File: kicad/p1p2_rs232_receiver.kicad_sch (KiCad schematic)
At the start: 51 parts, among them J1 Raspberry_Pi_2_3, J2 PC MC_1,5_2-G-3.81, U1 LTV-817S, U2 LM317L_TO92, U3 Pico

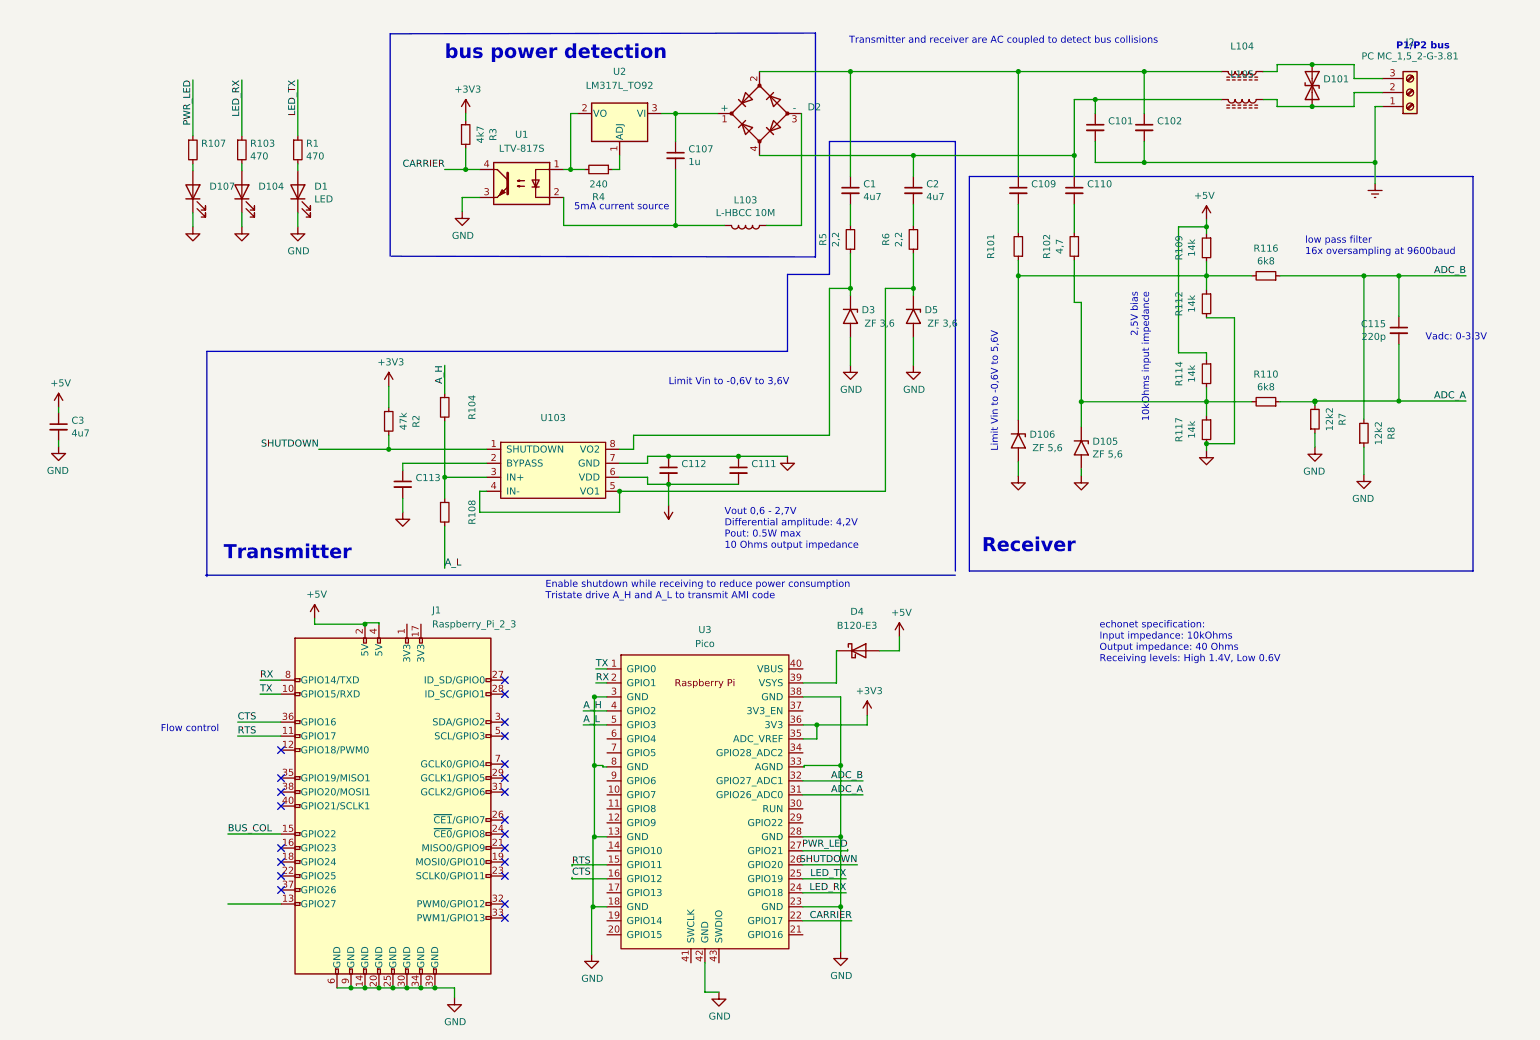
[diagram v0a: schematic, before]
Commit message: kicad: Minor fixes
Signed-off-by: Patrick Rudolph <rudolphpatrick05@gmail.com>
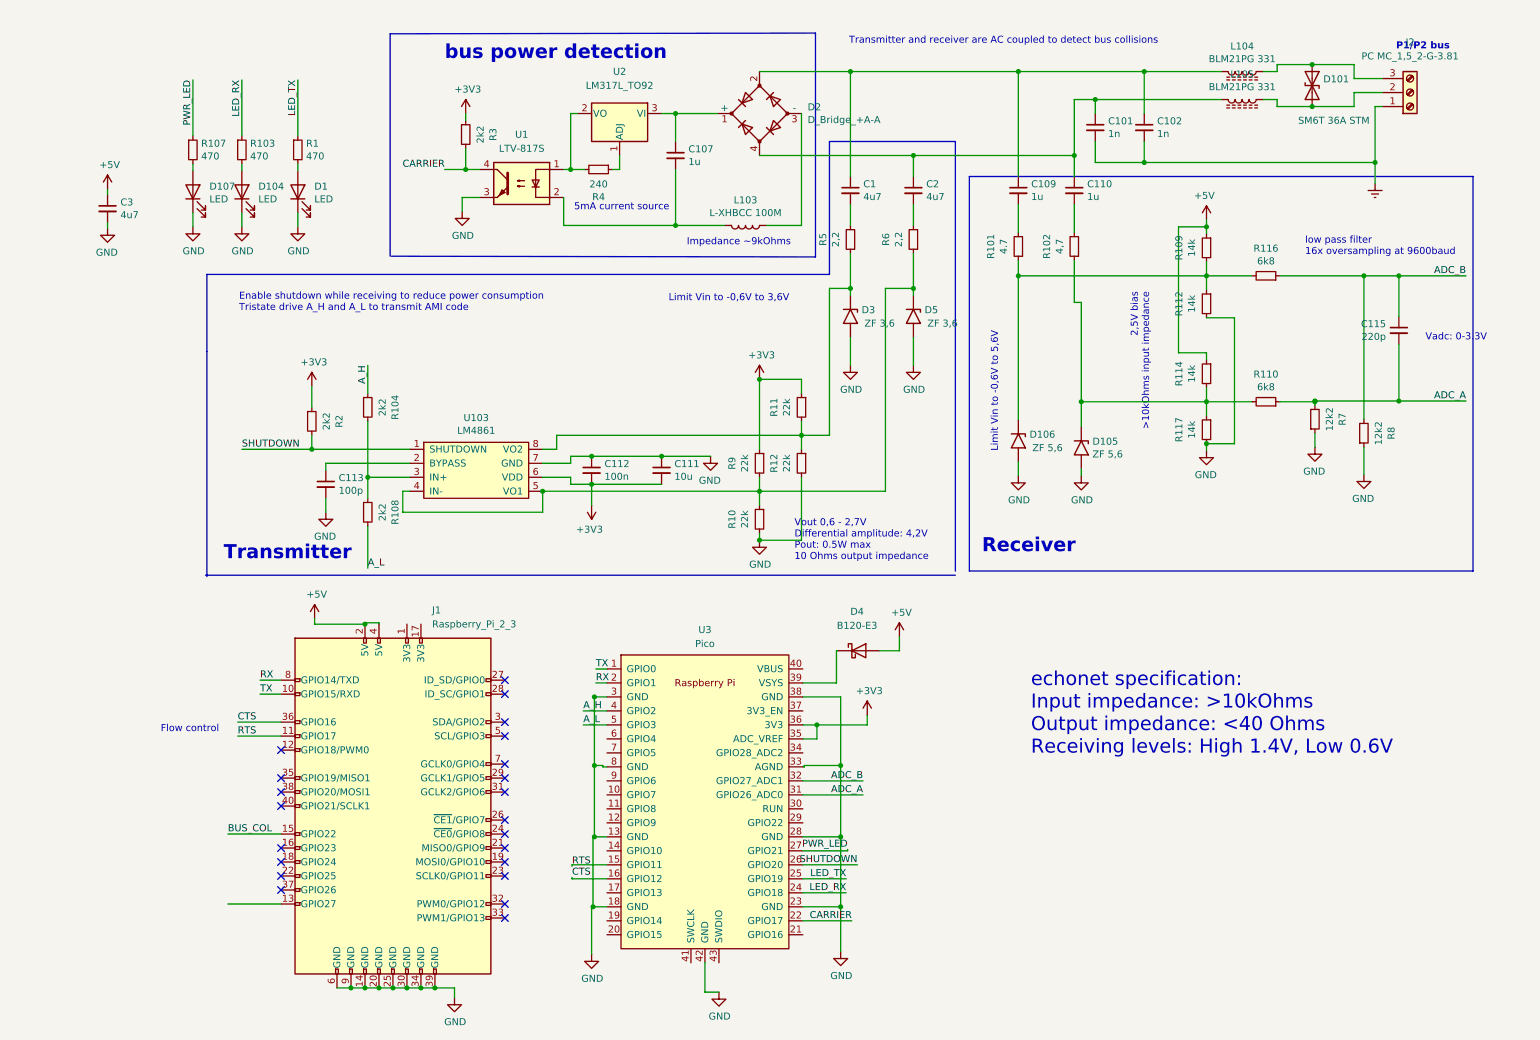
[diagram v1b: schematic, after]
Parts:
- added R10, R11, R12, R9: 22k, Resistor_SMD:R_0805_2012Metric_Pad1.20x1.40mm_HandSolder, symbol Device:R_Small
- C101, C102: value (none) -> 1n; footprint (none) -> Capacitor_SMD:C_0603_1608Metric_Pad1.08x0.95mm_HandSolder
- C109, C110: value (none) -> 1u; footprint (none) -> Capacitor_SMD:C_1210_3225Metric_Pad1.33x2.70mm_HandSolder
- C111: value (none) -> 10u; footprint (none) -> Capacitor_SMD:C_1210_3225Metric_Pad1.33x2.70mm_HandSolder
- C112: value (none) -> 100n; footprint (none) -> Capacitor_SMD:C_0805_2012Metric_Pad1.18x1.45mm_HandSolder
- C113: value (none) -> 100p; footprint (none) -> Capacitor_SMD:C_0603_1608Metric_Pad1.08x0.95mm_HandSolder
- D101: value (none) -> SM6T 36A STM; footprint (none) -> Diode_SMD:D_SMB
- D104, D107: value (none) -> LED; footprint (none) -> LED_SMD:LED_0805_2012Metric_Pad1.15x1.40mm_HandSolder
- D2: value (none) -> D_Bridge_+A-A; footprint (none) -> Diode_THT:Diode_Bridge_Round_D9.0mm
- L103: value L-HBCC 10M -> L-XHBCC 100M
- L104, L105: value (none) -> BLM21PG 331; footprint (none) -> Inductor_SMD:L_0805_2012Metric_Pad1.15x1.40mm_HandSolder
- R101: value (none) -> 4.7; footprint (none) -> Resistor_SMD:R_1206_3216Metric_Pad1.30x1.75mm_HandSolder
- R104, R108: value (none) -> 2k2; footprint (none) -> Resistor_SMD:R_0805_2012Metric_Pad1.20x1.40mm_HandSolder
- R107: value (none) -> 470; footprint (none) -> Resistor_SMD:R_0805_2012Metric_Pad1.20x1.40mm_HandSolder
- R2: value 47k -> 2k2
- R3: value 4k7 -> 2k2
- U103: value (none) -> LM4861
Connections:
- net +3V3: now also R11.1, R9.1
- net GND: now also R10.2, R12.2
- net at D5.1 (A1), R6.1, U103.4 (IN-)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: now also R10.1, R9.2
- net at D3.1 (A1), R5.1, U103.8 (VO2): now also R11.2, R12.1
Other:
- note added: "2,5V bias >10kOhms input impedance"
- note added: "Impedance ~9kOhms"
- note added: "echonet specification: Input impedance: >10kOhms Output impedance: <40 Ohms Receiving levels: High 1.4V, Low 0.6V"
- note removed: "2,5V bias 10kOhms input impedance"
- note removed: "echonet specification: Input impedance: 10kOhms Output impedance: 40 Ohms Receiving levels: High 1.4V, Low 0.6V"
- moved on the sheet: C111, C112, C113, C3, R104, R108, R2, U103

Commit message: kicad: Update schematics
- Add common mode choke
- Use gain 5 for OpAmp
  The OpAmp is not stable at unity gain.
  The OpAmp is not stable with high impedance load (unconnected P1/P2 bus).
- Use OpAmp in inverting operation mode instead voltage follower mode
- Add 'DNP' pull down and capacitor on OpAmp feedback
  TODO: Figure out if required for stability.
- Replace DC bus level detection
- Use external precision 3.0V voltage shunt as ADC voltage
- Use 3.0V as bias voltage to reduce noise
- Add Pico reset button

Signed-off-by: Patrick Rudolph <rudolphpatrick05@gmail.com>
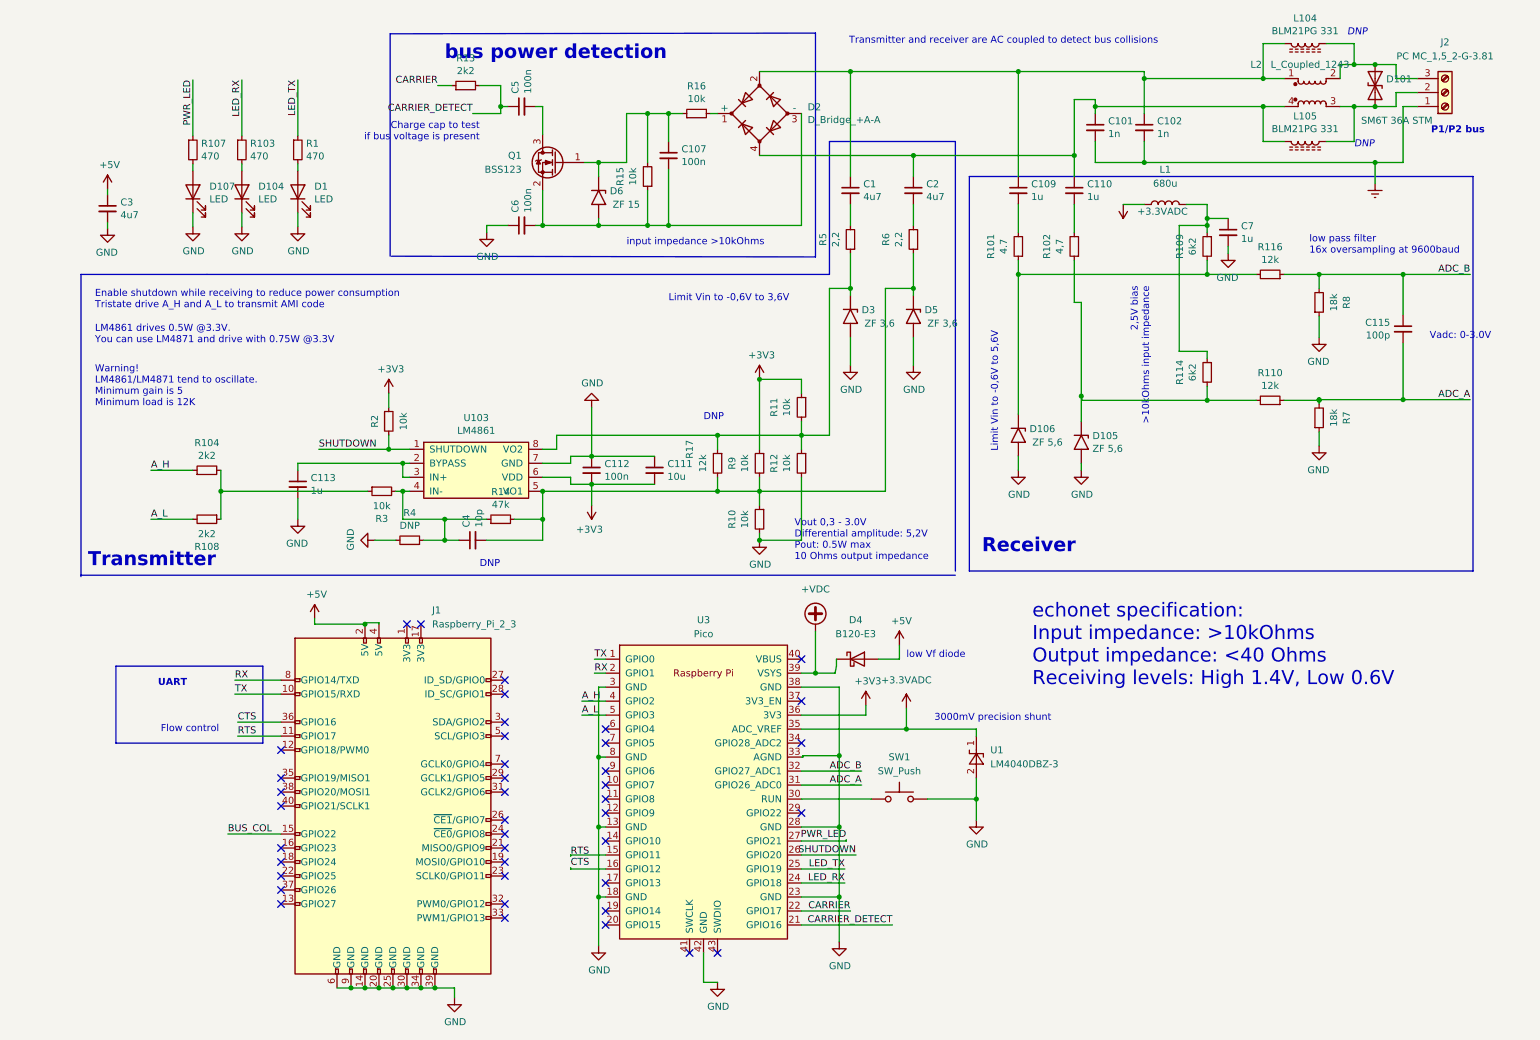
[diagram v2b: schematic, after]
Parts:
- removed L103: L-XHBCC 100M, Inductor_THT:L_Axial_L14.0mm_D4.5mm_P5.08mm_Vertical_Fastron_LACC, symbol Device:L
- removed R112, R117: 14k, Resistor_SMD:R_0805_2012Metric_Pad1.20x1.40mm_HandSolder, symbol Device:R_Small
- removed U1: LTV-817S, Package_DIP:SMDIP-4_W9.53mm, symbol Isolator:LTV-817S
- removed U2: LM317L_TO92, Package_TO_SOT_THT:TO-92_Inline, symbol Regulator_Linear:LM317L_TO92
- added C4: 10p, Capacitor_SMD:C_0805_2012Metric_Pad1.18x1.45mm_HandSolder, symbol Device:C_Small
- added C5, C6: 100n, Capacitor_SMD:C_0805_2012Metric_Pad1.18x1.45mm_HandSolder, symbol Device:C_Small
- added C7: 1u, Capacitor_SMD:C_1210_3225Metric_Pad1.33x2.70mm_HandSolder, symbol Device:C_Small
- added D6: ZF 15, Diode_THT:D_5W_P5.08mm_Vertical_AnodeUp, symbol Diode:SM6T24A
- added L1: 680u, Inductor_SMD:L_1210_3225Metric_Pad1.42x2.65mm_HandSolder, symbol Device:L
- added L2: L_Coupled_1243, B82790C0:L_CommonMode_TDK_B82790C0, symbol Device:L_Coupled_1243
- added Q1: BSS123, Package_TO_SOT_SMD:SOT-23, symbol Transistor_FET:BSS123
- added R13: 2k2, Resistor_SMD:R_0805_2012Metric_Pad1.20x1.40mm_HandSolder, symbol Device:R_Small
- added R14: 47k, Resistor_SMD:R_0805_2012Metric_Pad1.20x1.40mm_HandSolder, symbol Device:R_Small
- added R15, R16: 10k, Resistor_SMD:R_0805_2012Metric_Pad1.20x1.40mm_HandSolder, symbol Device:R_Small
- added R17: 12k, Resistor_SMD:R_0805_2012Metric_Pad1.20x1.40mm_HandSolder, symbol Device:R_Small
- added SW1: SW_Push, Button_Switch_THT:SW_PUSH_6mm_H5mm, symbol Switch:SW_Push
- added U1: LM4040DBZ-3, Package_TO_SOT_SMD:SOT-23, symbol Reference_Voltage:LM4040DBZ-3
- C107: value 1u -> 100n; footprint Capacitor_SMD:C_1206_3216Metric_Pad1.33x1.80mm_HandSolder -> Capacitor_SMD:C_0805_2012Metric_Pad1.18x1.45mm_HandSolder
- C113: value 100p -> 1u
- C115: value 220p -> 100p
- R10, R11, R12, R9: value 22k -> 10k
- R101, R102, R5, R6: footprint Resistor_SMD:R_1206_3216Metric_Pad1.30x1.75mm_HandSolder -> Resistor_SMD:R_0805_2012Metric_Pad1.20x1.40mm_HandSolder
- R109, R114: value 14k -> 6k2
- R110, R116: value 6k8 -> 12k
- R2, R3: value 2k2 -> 10k
- R4: value 240 -> DNP
- R7, R8: value 12k2 -> 18k
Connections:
- net +3V3: no longer R3.1, U3.35 (ADC_VREF)
- net +5V: no longer R109.1, R114.1
- net CARRIER: now also R13.1; no longer R3.2
- net GND: now also R4.2, C6.1, C7.2, SW1.2, U1.2 (A)
- net at D2.1 (+): now also R16.2; no longer C107.1
- net at C1.1, C102.1, C109.1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: now also L2.1
- net at D2.3 (-): now also C107.2, C6.2, D6.2 (A2), Q1.2 (S), R15.1
- net at C101.1, C110.1, C2.1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: now also L2.4
- net at D101.1 (A1), J2.3 (Pin_3), L104.1: now also L2.2
- net at D101.2 (A2), J2.2 (Pin_2), L105.1: now also L2.3
- net at C113.1, U103.2 (BYPASS): now also U103.3 (IN+)
- net at R104.2, R108.1: now also R3.1; no longer U103.3 (IN+)
- net at D5.1 (A1), R10.1, R6.1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: now also C4.2, R14.2, R17.2; no longer U103.4 (IN-)
- net at D3.1 (A1), R11.2, R12.1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: now also R17.1
- net at R4.1: now also R3.2, U103.4 (IN-), C4.1, R14.1
- net +VDC: now reaches D4.1 (K), U3.39 (VSYS)
- net CARRIER_DETECT: now reaches U3.21 (GPIO16)
- net CARRIER_DETECT: now also C5.1, R13.2
- net at U3.30 (RUN): now also SW1.1
- new net: C7.1, L1.2, R109.1, R114.1
- new net: C107.1, D6.1 (A1), Q1.1 (G), R15.2, R16.1
- new net: C5.2, Q1.3 (D)
- new net +3.3VADC: L1.1, U1.1 (K), U3.35 (ADC_VREF)
- no-connect marks 22 -> 41
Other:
- note added: "3000mV precision shunt"
- note added: "Charge cap to test if bus voltage is present"
- note added: "DNP"
- note added: "LM4861 drives 0.5W @3.3V. You can use LM4871 and drive with 0.75W @3.3V"
- note added: "UART"
- note added: "Vadc: 0-3.0V"
- note added: "Vout 0,3 - 3.0V Differential amplitude: 5,2V Pout: 0.5W max 10 Ohms output impedance"
- note added: "Warning! LM4861/LM4871 tend to oscillate. Minimum gain is 5 Minimum load is 12K"
- note added: "input impedance >10kOhms"
- note added: "low Vf diode"
- note removed: "5mA current source"
- note removed: "Impedance ~9kOhms"
- note removed: "Vadc: 0-3.3V"
- note removed: "Vout 0,6 - 2,7V Differential amplitude: 4,2V Pout: 0.5W max 10 Ohms output impedance"
- moved on the sheet: C107, C111, C113, C115, D101, D105, D106, D4, J2, L104, L105, R104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

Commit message: kicad: Update schematic
Signed-off-by: Patrick Rudolph <rudolphpatrick05@gmail.com>
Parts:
- C4: value 10p -> 4p7
- D105, D106, D3, D5, D6: footprint Diode_THT:D_5W_P5.08mm_Vertical_AnodeUp -> Diode_THT:D_DO-41_SOD81_P5.08mm_Vertical_AnodeUp
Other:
- note added: "Add 4p7 to prevent oscillation"
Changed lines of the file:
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@@
     (effects (font (size 1.27 1.27)) (justify left bottom))
   )
-  (text "DNP" (at 99.06 114.3 0)
+  (text "Add 4p7 to prevent oscillation" (at 99.06 114.3 0)
     (effects (font (size 1.27 1.27)) (justify left bottom))
   )
@@
       (effects (font (size 1.27 1.27)) (justify left))
     )
-    (property "Footprint" "Diode_THT:D_5W_P5.08mm_Vertical_AnodeUp" (id 2) (at 203.2 91.44 0)
+    (property "Footprint" "Diode_THT:D_DO-41_SOD81_P5.08mm_Vertical_AnodeUp" (id 2) (at 203.2 91.44 0)
       (effects (font (size 1.27 1.27)) hide)
     )
@@
       (effects (font (size 1.27 1.27)) (justify left))
     )
-    (property "Footprint" "Diode_THT:D_5W_P5.08mm_Vertical_AnodeUp" (id 2) (at 191.77 90.17 0)
+    (property "Footprint" "Diode_THT:D_DO-41_SOD81_P5.08mm_Vertical_AnodeUp" (id 2) (at 191.77 90.17 0)
       (effects (font (size 1.27 1.27)) hide)
     )
@@
       (effects (font (size 1.27 1.27)) (justify left))
     )
-    (property "Value" "10p" (id 1) (at 98.933 106.8832 0)
+    (property "Value" "4p7" (id 1) (at 98.933 106.8832 0)
       (effects (font (size 1.27 1.27)) (justify left))
     )
@@
       (effects (font (size 1.27 1.27)) (justify left))
     )
-    (property "Footprint" "Diode_THT:D_5W_P5.08mm_Vertical_AnodeUp" (id 2) (at 172.72 68.58 0)
+    (property "Footprint" "Diode_THT:D_DO-41_SOD81_P5.08mm_Vertical_AnodeUp" (id 2) (at 172.72 68.58 0)
       (effects (font (size 1.27 1.27)) hide)
     )
@@
       (effects (font (size 1.27 1.27)) (justify left))
     )
-    (property "Footprint" "Diode_THT:D_5W_P5.08mm_Vertical_AnodeUp" (id 2) (at 161.29 68.58 0)
+    (property "Footprint" "Diode_THT:D_DO-41_SOD81_P5.08mm_Vertical_AnodeUp" (id 2) (at 161.29 68.58 0)
       (effects (font (size 1.27 1.27)) hide)
     )
@@
       (effects (font (size 1.27 1.27)) (justify left))
     )
-    (property "Footprint" "Diode_THT:D_5W_P5.08mm_Vertical_AnodeUp" (id 2) (at 115.57 46.99 0)
+    (property "Footprint" "Diode_THT:D_DO-41_SOD81_P5.08mm_Vertical_AnodeUp" (id 2) (at 115.57 46.99 0)
       (effects (font (size 1.27 1.27)) hide)
     )
@@
     )
     (path "/3e4c5d80-d949-4992-89fb-dfed2a253e2f"
-      (reference "C4") (unit 1) (value "10p") (footprint "Capacitor_SMD:C_0805_2012Metric_Pad1.18x1.45mm_HandSolder")
+      (reference "C4") (unit 1) (value "4p7") (footprint "Capacitor_SMD:C_0805_2012Metric_Pad1.18x1.45mm_HandSolder")
     )
     (path "/b974de0b-ab88-4a84-a58b-0ff122d4436f"
@@
     )
     (path "/922c4491-769e-4fe6-b6eb-b5231440d121"
-      (reference "D3") (unit 1) (value "ZF 3,6") (footprint "Diode_THT:D_5W_P5.08mm_Vertical_AnodeUp")
+      (reference "D3") (unit 1) (value "ZF 3,6") (footprint "Diode_THT:D_DO-41_SOD81_P5.08mm_Vertical_AnodeUp")
     )
     (path "/41fb219b-dbb3-45ba-81ff-2e18031ac973"
@@
     )
     (path "/8867f2d2-007b-483f-a02e-b58e041d28b1"
-      (reference "D5") (unit 1) (value "ZF 3,6") (footprint "Diode_THT:D_5W_P5.08mm_Vertical_AnodeUp")
+      (reference "D5") (unit 1) (value "ZF 3,6") (footprint "Diode_THT:D_DO-41_SOD81_P5.08mm_Vertical_AnodeUp")
     )
     (path "/b9ae78e7-5f4e-4976-833d-d7fdf199aea3"
-      (reference "D6") (unit 1) (value "ZF 15") (footprint "Diode_THT:D_5W_P5.08mm_Vertical_AnodeUp")
+      (reference "D6") (unit 1) (value "ZF 15") (footprint "Diode_THT:D_DO-41_SOD81_P5.08mm_Vertical_AnodeUp")
     )
     (path "/00000000-0000-0000-0000-0000624e2476"
@@
     )
     (path "/00000000-0000-0000-0000-0000624e249b"
-      (reference "D105") (unit 1) (value "ZF 5,6") (footprint "Diode_THT:D_5W_P5.08mm_Vertical_AnodeUp")
+      (reference "D105") (unit 1) (value "ZF 5,6") (footprint "Diode_THT:D_DO-41_SOD81_P5.08mm_Vertical_AnodeUp")
     )
     (path "/00000000-0000-0000-0000-0000624e24a1"
-      (reference "D106") (unit 1) (value "ZF 5,6") (footprint "Diode_THT:D_5W_P5.08mm_Vertical_AnodeUp")
+      (reference "D106") (unit 1) (value "ZF 5,6") (footprint "Diode_THT:D_DO-41_SOD81_P5.08mm_Vertical_AnodeUp")
     )
     (path "/00000000-0000-0000-0000-000062526ce2"
